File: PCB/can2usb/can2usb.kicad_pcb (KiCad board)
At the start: 2 copper layers, 36 parts, among them J1 STLINK, J2 Conn_01x03_Male, P1 USB_C_Plug_USB2.0, SW1 BOOT_SW, U1 STM32F103C6Tx, U2 TLP175A, U3 MCP2561-E-SN, U4 LM1117-3.3, U5 USBLC6-2SC6, Y1 16MHz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

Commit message: First version pcb
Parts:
- removed R8: 1k, Resistor_SMD:R_0805_2012Metric
- removed SW1: BOOT_SW, Button_Switch_SMD:SW_SPDT_PCM12
- C10, C5, C6, C7, C8, R1, R_CONF1, U1, U5, Y1, Y2: moved to B.Cu
- R_Terminator1, U2, U3, U4: moved to F.Cu
- moved U1 79.7 mm to (89.0, 58.3)
- moved C3 77.3 mm to (96.6, 57.3), turned to 90 degrees
- moved C2 75.4 mm to (99.2, 57.3), turned to 90 degrees
- moved C10 74.8 mm to (97.8, 51.8), turned to 90 degrees
- moved C1 71.2 mm to (101.7, 57.3), turned to 90 degrees
- moved C9 71.0 mm to (104.5, 48.1), turned to 180 degrees
- moved C4 68.9 mm to (94.1, 57.3), turned to 90 degrees
- moved J1 65.8 mm to (104.8, 61.2), turned to 270 degrees
- moved U3 64.4 mm to (78.6, 62.2), turned to 180 degrees
- moved C7 64.2 mm to (83.3, 63.2)
- moved U2 62.6 mm to (69.3, 59.3)
- moved R2 59.7 mm to (87.0, 50.0), turned to 270 degrees
- moved J2 59.5 mm to (72.0, 52.5), turned to 270 degrees
- moved D1 59.1 mm to (86.5, 46.7)
- moved C8 58.9 mm to (79.6, 63.4)
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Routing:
- net GND: track 0.00 -> 140.0 mm, vias 0 -> 4
- net +3V3: track 0.00 -> 77.0 mm, vias 0 -> 6
- net +5V: track 0.00 -> 50.5 mm, vias 0 -> 1
- net CAN_H: track 0.00 -> 15.2 mm, vias 0 -> 1
- net USB_D-: track 0.00 -> 13.3 mm
- net USB_D+: track 0.00 -> 12.7 mm
- net CAN_L: track 0.00 -> 12.4 mm, vias 0 -> 1
- net OSC_IN: track 0.00 -> 12.4 mm
- net SWCLK: track 0.00 -> 11.0 mm
- net B_LED: track 0.00 -> 10.5 mm, vias 0 -> 1
- net L_OSC_OUT: track 0.00 -> 10.1 mm
- net Net-(R5-Pad2): track 0.00 -> 9.70 mm
- net OSC_OUT: track 0.00 -> 8.65 mm
- net CAN_RX: track 0.00 -> 8.13 mm, vias 0 -> 1
- net CAN_TX: track 0.00 -> 7.73 mm, vias 0 -> 1
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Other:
- board text added: "CAN"
- board text added: "CLK"
- board text added: "GND"
- board text added: "IO"
- board text added: "SYS"
- board text added: "UART"

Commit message: Finished brd
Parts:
- added H1: MountingHole, MountingHole:MountingHole_2.2mm_M2, F.Cu at (67.7, 47.2)
- added H2: MountingHole, MountingHole:MountingHole_2.2mm_M2, F.Cu at (109.7, 47.2)
- added H3: MountingHole, MountingHole:MountingHole_2.2mm_M2, F.Cu at (109.7, 63.2)
- added JP1: SolderJumper_3_Open, Jumper:SolderJumper-3_P1.3mm_Open_RoundedPad1.0x1.5mm, B.Cu at (88.6, 48.5)
- added R8: 1k, Resistor_SMD:R_0805_2012Metric, B.Cu at (90.3, 50.8)
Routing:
- net GND: track 140.0 -> 174.9 mm, vias 4 -> 5
- net TERMINATOR_SW: track 0.00 -> 16.6 mm, vias 0 -> 1
- net Net-(P1-PadS1): track 0.00 -> 15.4 mm
- net BOOT0: track 0.00 -> 12.9 mm, vias 0 -> 2
- net +3V3: track 77.0 -> 89.1 mm
- net Net-(F1-Pad1): track 9.90 -> 16.6 mm
- net Net-(JP1-Pad2): track 0.00 -> 2.61 mm
- added copper zone on B.Cu, net GND
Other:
- board outline added: 58.5 x 22.2 mm
- board text added: "By K. Pergol"
- board text added: "By Karol Pergol"
- board text added: "USB2CAN"

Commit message: Minor chnages
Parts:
- moved H3 0.50 mm to (109.7, 62.7)
- renumbered J2 to CAN, R_Terminator1 to R_TERM
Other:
- board text added: "CANH"
- board text added: "CANL"
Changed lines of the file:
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@@
   (general
     (thickness 1.6)
-    (drawings 29)
+    (drawings 32)
     (tracks 300)
     (zones 0)
@@
       (effects (font (size 1 1) (thickness 0.15)) (justify mirror))
     )
-    (fp_text user %R (at 0 0) (layer B.Fab)
-      (effects (font (size 0.5 0.5) (thickness 0.08)) (justify mirror))
-    )
     (fp_line (start -1 -0.625) (end -1 0.625) (layer B.Fab) (width 0.1))
     (fp_line (start -1 0.625) (end 1 0.625) (layer B.Fab) (width 0.1))
@@
     (fp_line (start 1.68 0.95) (end 1.68 -0.95) (layer B.CrtYd) (width 0.05))
     (fp_line (start 1.68 -0.95) (end -1.68 -0.95) (layer B.CrtYd) (width 0.05))
+    (fp_text user %R (at 0 0) (layer B.Fab)
+      (effects (font (size 0.5 0.5) (thickness 0.08)) (justify mirror))
+    )
     (pad 2 smd roundrect (at 0.9125 0 180) (size 1.025 1.4) (layers B.Cu B.Paste B.Mask) (roundrect_rratio 0.243902)
       (net 33 "Net-(JP1-Pad2)"))
@@
       (effects (font (size 1 1) (thickness 0.15)) (justify mirror))
     )
-    (fp_arc (start -1.35 0.3) (end -1.35 1) (angle 90) (layer B.SilkS) (width 0.12))
-    (fp_arc (start -1.35 -0.3) (end -2.05 -0.3) (angle 90) (layer B.SilkS) (width 0.12))
-    (fp_arc (start 1.35 -0.3) (end 1.35 -1) (angle 90) (layer B.SilkS) (width 0.12))
-    (fp_arc (start 1.35 0.3) (end 2.05 0.3) (angle 90) (layer B.SilkS) (width 0.12))
     (fp_line (start -1.2 -1.2) (end -0.9 -1.5) (layer B.SilkS) (width 0.12))
     (fp_line (start -1.5 -1.5) (end -0.9 -1.5) (layer B.SilkS) (width 0.12))
@@
     (fp_line (start 2.3 -1.25) (end 2.3 1.25) (layer B.CrtYd) (width 0.05))
     (fp_line (start 2.3 -1.25) (end -2.3 -1.25) (layer B.CrtYd) (width 0.05))
+    (fp_arc (start -1.35 0.3) (end -1.35 1) (angle 90) (layer B.SilkS) (width 0.12))
+    (fp_arc (start -1.35 -0.3) (end -2.05 -0.3) (angle 90) (layer B.SilkS) (width 0.12))
+    (fp_arc (start 1.35 -0.3) (end 1.35 -1) (angle 90) (layer B.SilkS) (width 0.12))
+    (fp_arc (start 1.35 0.3) (end 2.05 0.3) (angle 90) (layer B.SilkS) (width 0.12))
     (pad 2 smd rect (at 0 0 180) (size 1 1.5) (layers B.Cu B.Mask)
       (net 33 "Net-(JP1-Pad2)"))
@@
   )
   (module MountingHole:MountingHole_2.2mm_M2 (layer F.Cu)
-    (at 109.691 63.244)
+    (at 109.691 62.744)
     (descr "Mounting Hole 2.2mm, no annular, M2")
     (tags "mounting hole 2.2mm no annular m2")
@@
       (effects (font (size 1 1) (thickness 0.15)))
     )
-    (fp_text user %R (at 0.3 0) (layer F.Fab)
-      (effects (font (size 1 1) (thickness 0.15)))
-    )
     (fp_circle (center 0 0) (end 2.2 0) (layer Cmts.User) (width 0.15))
     (fp_circle (center 0 0) (end 2.45 0) (layer F.CrtYd) (width 0.05))
+    (fp_text user %R (at 0.3 0) (layer F.Fab)
+      (effects (font (size 1 1) (thickness 0.15)))
+    )
     (pad 1 np_thru_hole circle (at 0 0) (size 2.2 2.2) (drill 2.2) (layers *.Cu *.Mask))
   )
@@
       (effects (font (size 1 1) (thickness 0.15)))
     )
-    (fp_text user %R (at 0.3 0) (layer F.Fab)
-      (effects (font (size 1 1) (thickness 0.15)))
-    )
     (fp_circle (center 0 0) (end 2.2 0) (layer Cmts.User) (width 0.15))
     (fp_circle (center 0 0) (end 2.45 0) (layer F.CrtYd) (width 0.05))
+    (fp_text user %R (at 0.3 0) (layer F.Fab)
+      (effects (font (size 1 1) (thickness 0.15)))
+    )
     (pad 1 np_thru_hole circle (at 0 0) (size 2.2 2.2) (drill 2.2) (layers *.Cu *.Mask))
   )
@@
     (tags "mounting hole 2.2mm no annular m2")
     (attr virtual)
-    (fp_text reference H1 (at -1.016 1.778) (layer F.SilkS)
+    (fp_text reference H1 (at -1.651 -1.905) (layer F.SilkS)
       (effects (font (size 1 1) (thickness 0.15)))
     )
     (fp_text value MountingHole (at 0 3.2) (layer F.Fab)
-      (effects (font (size 1 1) (thickness 0.15)))
-    )
-    (fp_text user %R (at 0.3 0) (layer F.Fab)
       (effects (font (size 1 1) (thickness 0.15)))
     )
     (fp_circle (center 0 0) (end 2.2 0) (layer Cmts.User) (width 0.15))
     (fp_circle (center 0 0) (end 2.45 0) (layer F.CrtYd) (width 0.05))
+    (fp_text user %R (at 0.3 0) (layer F.Fab)
+      (effects (font (size 1 1) (thickness 0.15)))
+    )
     (pad 1 np_thru_hole circle (at 0 0) (size 2.2 2.2) (drill 2.2) (layers *.Cu *.Mask))
   )
@@
     (tags SOT-23-6)
     (attr smd)
-    (fp_text reference U5 (at 0 2.9) (layer B.SilkS)
+    (fp_text reference U5 (at 2.921 -0.127) (layer B.SilkS)
       (effects (font (size 1 1) (thickness 0.15)) (justify mirror))
     )
@@
     (descr "Through hole straight pin header, 1x03, 2.54mm pitch, single row")
     (tags "Through hole pin header THT 1x03 2.54mm single row")
-    (fp_text reference J2 (at 0 -2.33 270) (layer F.SilkS)
+    (fp_text reference CAN (at 2.54 2.413) (layer F.SilkS)
       (effects (font (size 1 1) (thickness 0.15)))
     )
@@
     (tags "CMS SOT")
     (attr smd)
-    (fp_text reference U4 (at 5.207 -1.905) (layer F.SilkS)
+    (fp_text reference U4 (at -0.127 4.064) (layer F.SilkS)
       (effects (font (size 1 1) (thickness 0.15)))
     )
@@
     (tags resistor)
     (attr smd)
-    (fp_text reference R_Terminator1 (at 2.159 -2.032) (layer F.SilkS)
-      (effects (font (size 1 1) (thickness 0.15)))
+    (fp_text reference R_TERM (at 0 -1.524) (layer F.SilkS)
+      (effects (font (size 0.6 0.6) (thickness 0.15)))
     )
     (fp_text value 100 (at 0 1.65) (layer F.Fab)
@@
     (tags resistor)
     (attr smd)
-    (fp_text reference R_CONF2 (at -0.635 -1.397) (layer F.SilkS)
-      (effects (font (size 1 1) (thickness 0.15)))
+    (fp_text reference R_CONF2 (at -0.127 -1.397) (layer F.SilkS)
+      (effects (font (size 0.6 0.6) (thickness 0.15)))
     )
     (fp_text value 1k5 (at 0 1.65) (layer F.Fab)
@@
     (tags resistor)
     (attr smd)
-    (fp_text reference R4 (at 0 -1.65 90) (layer F.SilkS)
+    (fp_text reference R4 (at 2.413 0 180) (layer F.SilkS)
       (effects (font (size 1 1) (thickness 0.15)))
     )
@@
     (tags resistor)
     (attr smd)
-    (fp_text reference R3 (at 0 -1.65 90) (layer F.SilkS)
+    (fp_text reference R3 (at 2.54 0 180) (layer F.SilkS)
       (effects (font (size 1 1) (thickness 0.15)))
     )
@@
     (tags resistor)
     (attr smd)
-    (fp_text reference R2 (at 0 -1.65 90) (layer F.SilkS)
+    (fp_text reference R2 (at 2.413 0.127 180) (layer F.SilkS)
       (effects (font (size 1 1) (thickness 0.15)))
     )
@@
     )
   )
+  (gr_text GND (at 66.802 50.165) (layer F.SilkS)
+    (effects (font (size 0.5 0.5) (thickness 0.1) italic))
+  )
+  (gr_text CANH (at 69.596 50.165) (layer F.SilkS)
+    (effects (font (size 0.5 0.5) (thickness 0.1) italic))
+  )
+  (gr_text CANL (at 72.136 50.165) (layer F.SilkS)
+    (effects (font (size 0.5 0.5) (thickness 0.1) italic))
+  )
   (gr_line (start 114.681 48.895) (end 120.904 48.895) (layer Edge.Cuts) (width 0.05))
   (gr_line (start 122.301 58.039) (end 122.301 50.292) (layer Edge.Cuts) (width 0.05))
@@
   (gr_line (start 113.284 47.498) (end 113.284 45.212) (layer Edge.Cuts) (width 0.05))
   (gr_arc (start 114.681 47.498) (end 113.284 47.498) (angle -90) (layer Edge.Cuts) (width 0.05))
-  (gr_text "By K. Pergol" (at 101.219 45.72) (layer F.SilkS)
-    (effects (font (size 1 1) (thickness 0.15)))
+  (gr_text "By K. Pergol" (at 74.93 46.99) (layer F.SilkS)
+    (effects (font (size 0.6 0.6) (thickness 0.125)))
   )
   (gr_line (start 111.76 66.04) (end 111.887 66.04) (layer Edge.Cuts) (width 0.05))
@@
   (gr_line (start 65.151 43.815) (end 104.14 43.815) (layer Edge.Cuts) (width 0.05))
   (gr_arc (start 65.151 45.212) (end 65.151 43.815) (angle -90) (layer Edge.Cuts) (width 0.05))
-  (gr_text USB2CAN (at 74.93 47.244) (layer F.SilkS)
-    (effects (font (size 1 1) (thickness 0.15)))
+  (gr_text USB2CAN (at 75.057 45.847) (layer F.SilkS)
+    (effects (font (size 1 1) (thickness 0.25)))
   )
   (gr_text "By Karol Pergol" (at 70.739 46.863) (layer B.Fab)

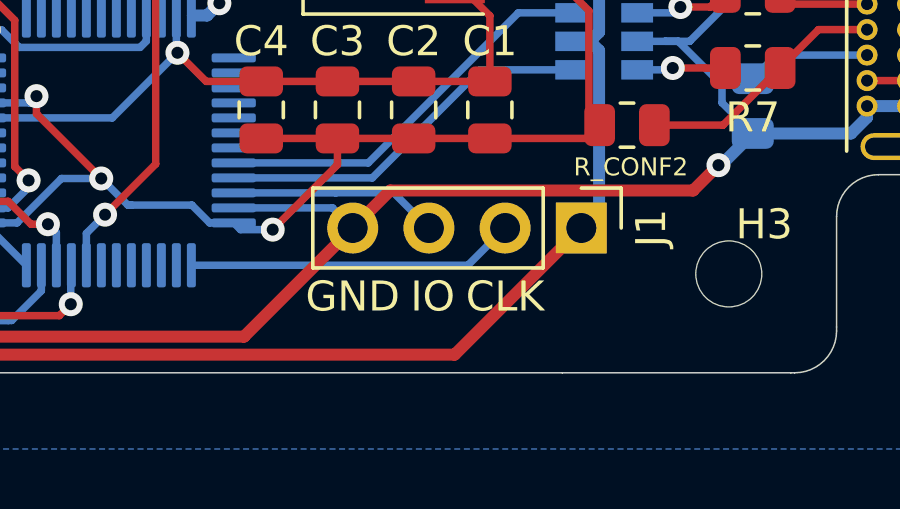
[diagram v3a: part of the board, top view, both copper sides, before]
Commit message: Minor chnages in PCB layout
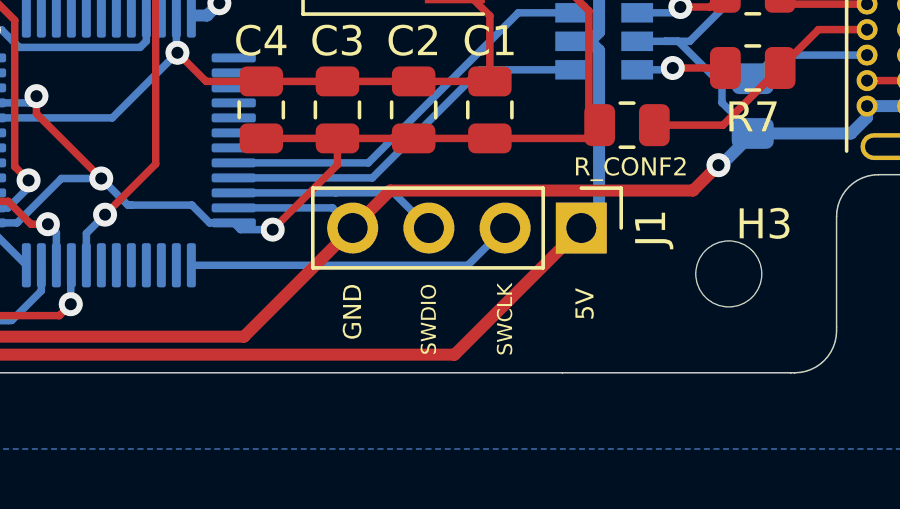
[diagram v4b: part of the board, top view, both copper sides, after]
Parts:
- renumbered JP1 to BOOT0
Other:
- board text added: "5V"
- board text added: "SWCLK"
- board text added: "SWDIO"
- board text removed: "CLK"
- board text removed: "IO"
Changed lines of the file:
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@@
   (general
     (thickness 1.6)
-    (drawings 32)
+    (drawings 33)
     (tracks 300)
     (zones 0)
@@
     (tags "solder jumper open")
     (attr virtual)
-    (fp_text reference JP1 (at 0 1.8) (layer B.SilkS)
-      (effects (font (size 1 1) (thickness 0.15)) (justify mirror))
+    (fp_text reference BOOT0 (at 0 1.8) (layer B.SilkS)
+      (effects (font (size 0.6 0.6) (thickness 0.1)) (justify mirror))
     )
     (fp_text value SolderJumper_3_Open (at 0 -1.9) (layer B.Fab)
@@
     )
   )
+  (gr_text 5V (at 104.902 63.754 90) (layer F.SilkS)
+    (effects (font (size 0.6 0.6) (thickness 0.15)))
+  )
   (gr_text GND (at 66.802 50.165) (layer F.SilkS)
     (effects (font (size 0.5 0.5) (thickness 0.1) italic))
@@
     (effects (font (size 1 1) (thickness 0.15)))
   )
-  (gr_text "GND\n" (at 97.155 63.5) (layer F.SilkS)
-    (effects (font (size 1 1) (thickness 0.15)))
-  )
-  (gr_text "CLK\n" (at 102.235 63.5) (layer F.SilkS)
-    (effects (font (size 1 1) (thickness 0.15)))
-  )
-  (gr_text "IO\n" (at 99.822 63.5) (layer F.SilkS)
-    (effects (font (size 1 1) (thickness 0.15)))
+  (gr_text "GND\n" (at 97.155 64.008 90) (layer F.SilkS)
+    (effects (font (size 0.6 0.6) (thickness 0.15)))
+  )
+  (gr_text "SWCLK\n" (at 102.235 64.262 90) (layer F.SilkS)
+    (effects (font (size 0.5 0.5) (thickness 0.125)))
+  )
+  (gr_text "SWDIO\n" (at 99.695 64.262 90) (layer F.SilkS)
+    (effects (font (size 0.5 0.5) (thickness 0.125)))
   )
   (gr_text "UART\n" (at 90.678 44.958) (layer F.SilkS)

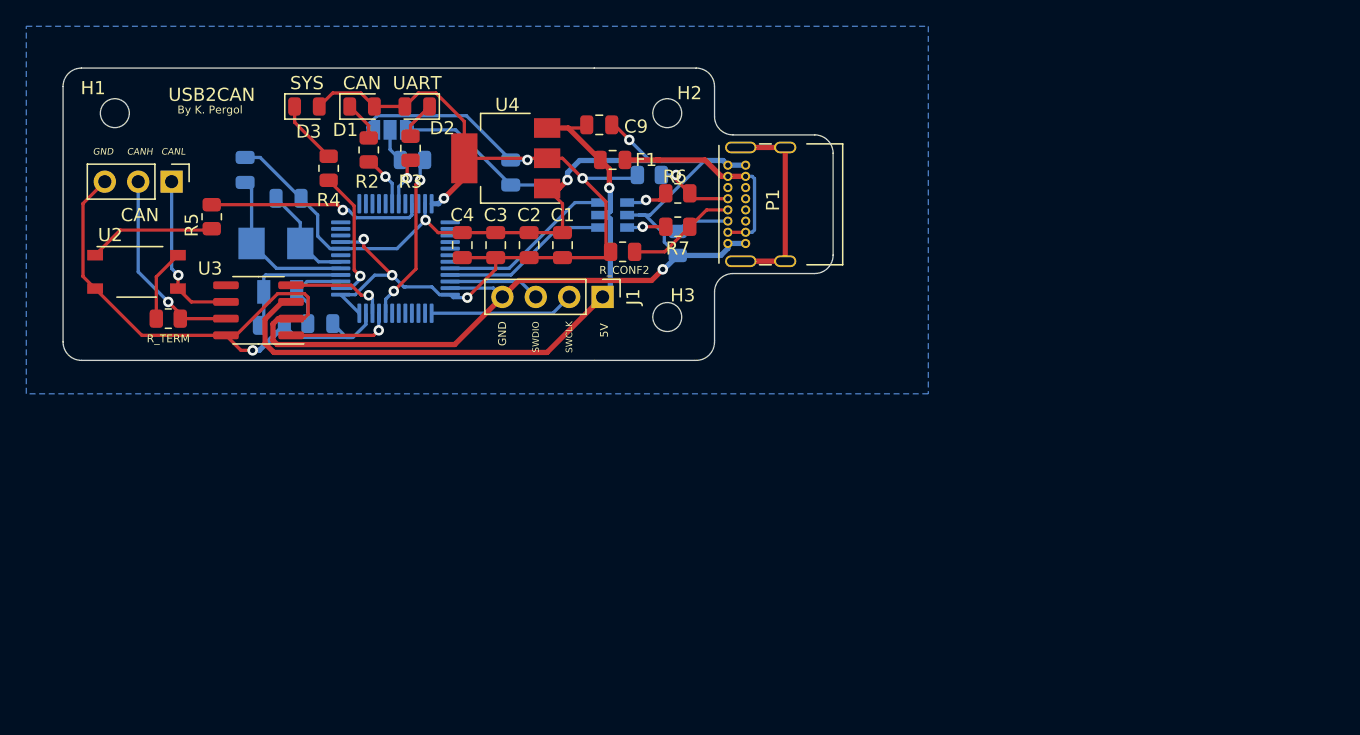
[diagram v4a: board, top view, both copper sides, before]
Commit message: New PCB design with 0402 and smaller LDO
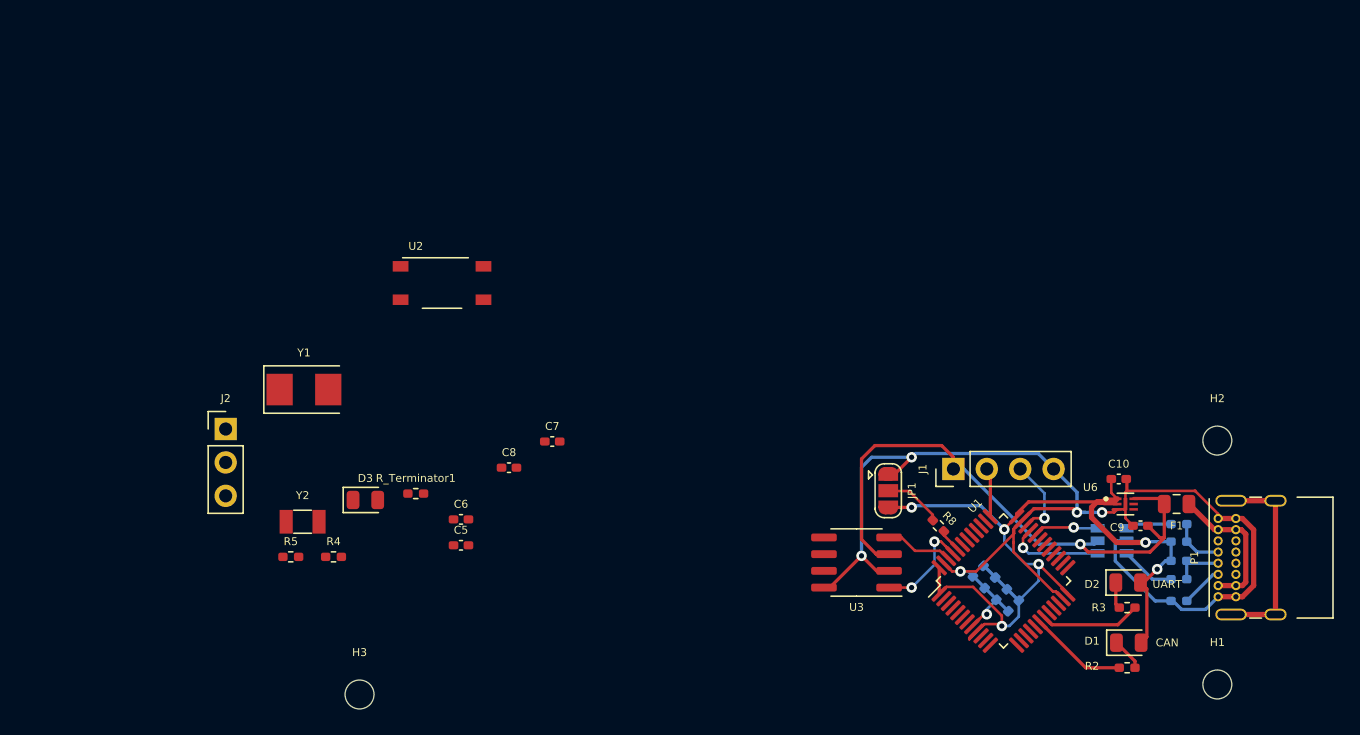
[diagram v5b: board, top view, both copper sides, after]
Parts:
- removed BOOT0: SolderJumper_3_Open, Jumper:SolderJumper-3_P1.3mm_Open_RoundedPad1.0x1.5mm
- removed CAN: Conn_01x03_Male, Connector_PinHeader_2.54mm:PinHeader_1x03_P2.54mm_Vertical
- removed R_TERM: 100, Resistor_SMD:R_0805_2012Metric
- removed U4: LM1117-3.3, Package_TO_SOT_SMD:SOT-223-3_TabPin2
- added J2: Conn_01x03_Male, Connector_PinHeader_2.54mm:PinHeader_1x03_P2.54mm_Vertical, F.Cu at (76.1, 71.3)
- added JP1: SolderJumper_3_Open, Jumper:SolderJumper-3_P1.3mm_Open_RoundedPad1.0x1.5mm, F.Cu at (126.5, 75.9)
- added R_Terminator1: 100, Resistor_SMD:R_0402_1005Metric_Pad0.72x0.64mm_HandSolder, F.Cu at (90.6, 76.2)
- added U6: MIC5528-3.3YMT-TR, can2usb:SON40P120X120X60-7N, F.Cu at (144.5, 77.0)
- C1, C2, C3, C4: footprint Capacitor_SMD:C_0805_2012Metric -> Capacitor_SMD:C_0402_1005Metric_Pad0.74x0.62mm_HandSolder; moved to B.Cu
- C10, C5, C6, C7, C8: footprint Capacitor_SMD:C_0805_2012Metric -> Capacitor_SMD:C_0402_1005Metric_Pad0.74x0.62mm_HandSolder; moved to F.Cu
- C9: footprint Capacitor_SMD:C_0805_2012Metric -> Capacitor_SMD:C_0402_1005Metric_Pad0.74x0.62mm_HandSolder
- R1, R2, R3, R4, R5, R_CONF1: footprint Resistor_SMD:R_0805_2012Metric -> Resistor_SMD:R_0402_1005Metric_Pad0.72x0.64mm_HandSolder
- R6, R7, R_CONF2: footprint Resistor_SMD:R_0805_2012Metric -> Resistor_SMD:R_0402_1005Metric_Pad0.72x0.64mm_HandSolder; moved to B.Cu
- R8: footprint Resistor_SMD:R_0805_2012Metric -> Resistor_SMD:R_0402_1005Metric_Pad0.72x0.64mm_HandSolder; moved to F.Cu
- U1, Y1, Y2: moved to F.Cu
- moved H1 94.4 mm to (151.5, 90.7)
- moved D1 71.1 mm to (144.8, 87.5)
- moved R2 69.8 mm to (144.7, 89.4), turned to 180 degrees
- moved D2 65.1 mm to (144.7, 82.9), turned to 0 degrees
- moved R3 64.7 mm to (144.7, 84.8), turned to 0 degrees
- moved U1 52.3 mm to (135.3, 82.8), turned to 45 degrees
- moved C10 51.8 mm to (144.0, 75.1), turned to 180 degrees
- moved C9 51.2 mm to (145.7, 78.6), turned to 0 degrees
- moved F1 50.2 mm to (148.4, 77.0)
- moved C4 50.1 mm to (136.0, 84.7), turned to 225 degrees
- moved U3 49.3 mm to (124.1, 81.4)
- moved R_CONF1 49.0 mm to (148.6, 79.8)
- moved R8 48.7 mm to (130.3, 78.6), turned to 135 degrees
- moved H2 48.7 mm to (151.5, 72.1)
- moved R_CONF2 48.4 mm to (148.6, 81.3)
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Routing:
- net GND: track 174.9 -> 103.6 mm, vias 5 -> 6
- net +3V3: track 89.1 -> 72.1 mm
- net TERMINATOR_SW: track 16.6 -> 0.00 mm, vias 1 -> 0
- net CAN_H: track 15.2 -> 0.00 mm, vias 1 -> 0
- net CAN_L: track 12.4 -> 0.00 mm, vias 1 -> 0
- net OSC_IN: track 12.4 -> 0.00 mm
- net BOOT0: track 12.9 -> 1.79 mm, vias 2 -> 0
- net B_LED: track 10.5 -> 0.00 mm, vias 1 -> 0
- net L_OSC_OUT: track 10.1 -> 0.00 mm
- net Net-(R5-Pad2): track 9.70 -> 0.00 mm
- net OSC_OUT: track 8.65 -> 0.00 mm
- net USB_D-: track 13.3 -> 5.78 mm, vias 0 -> 1
- net SWCLK: track 11.0 -> 3.73 mm
- net L_OSC_IN: track 6.44 -> 0.00 mm
- net +5V: track 50.5 -> 44.5 mm
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- removed copper zone on B.Cu, net GND
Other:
- board outline removed
- net class Small added: clearance 0.2, trace_width 0.2, via_dia 0.5, via_drill 0.4
- board text removed: "5V"
- board text removed: "By K. Pergol"
- board text removed: "By Karol Pergol"
- board text removed: "CANH"
- board text removed: "CANL"
- board text removed: "GND"
- board text removed: "SWCLK"
- board text removed: "SWDIO"
- board text removed: "SYS"
- board text removed: "USB2CAN"
